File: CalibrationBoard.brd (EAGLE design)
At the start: 100 x 80 mm, 113 parts, among them J1 BANANA_CONN, J2 BANANA_CONN, J3 BANANA_CONN, J4 BANANA_CONN, J5 BANANA_CONN, J6 BANANA_CONN, J7 BANANA_CONN, J8 BANANA_CONN, J9 BANANA_CONN, Q1 IRF540, U1 MAX6126AASA25+, U2 MAX6126AASA25+, U3 MAX6126AASA50+

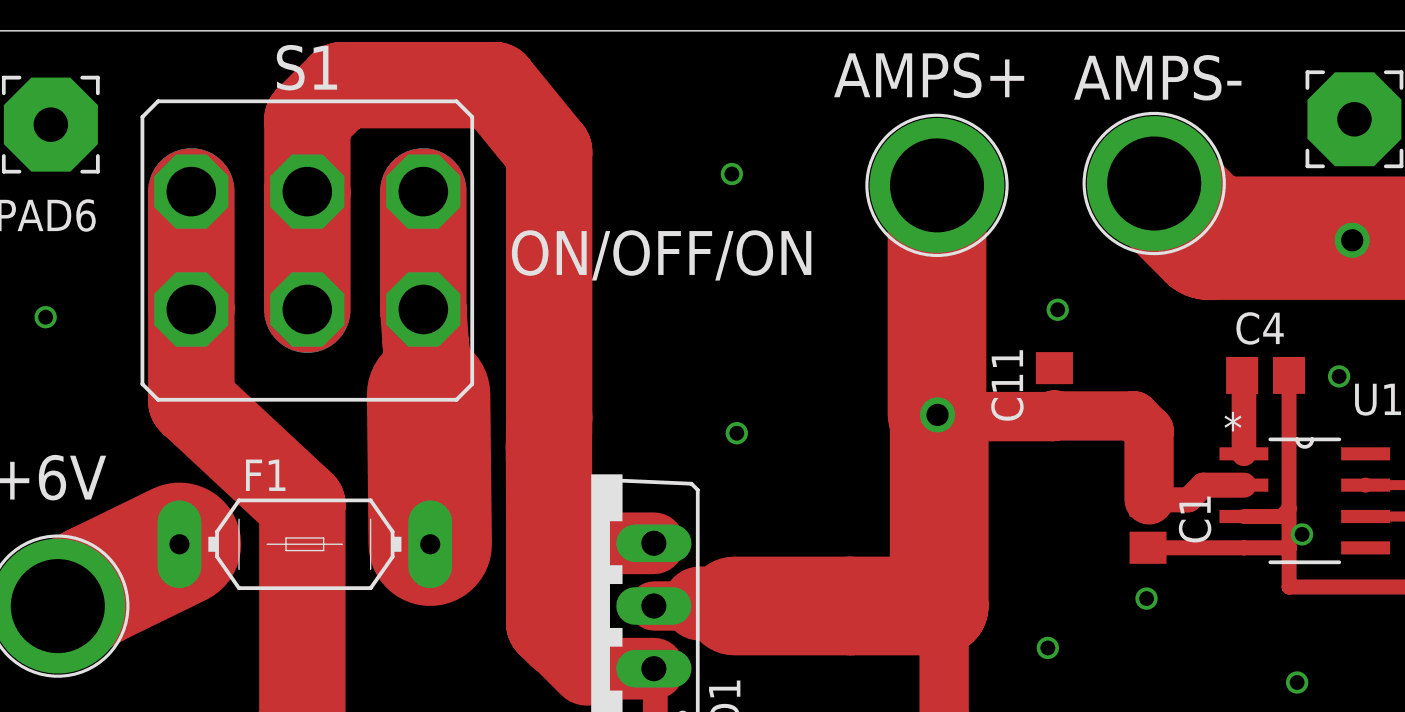
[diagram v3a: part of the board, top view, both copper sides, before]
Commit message: Various minor changes with minor CAD impacts
Connected some minor air nets (no CAD issues)
Changed NR caps from 1uF to 0.1uF as per DS.
Moved a decoupling cap to allow ground flood to IC.
Standardised the plane to track separation.
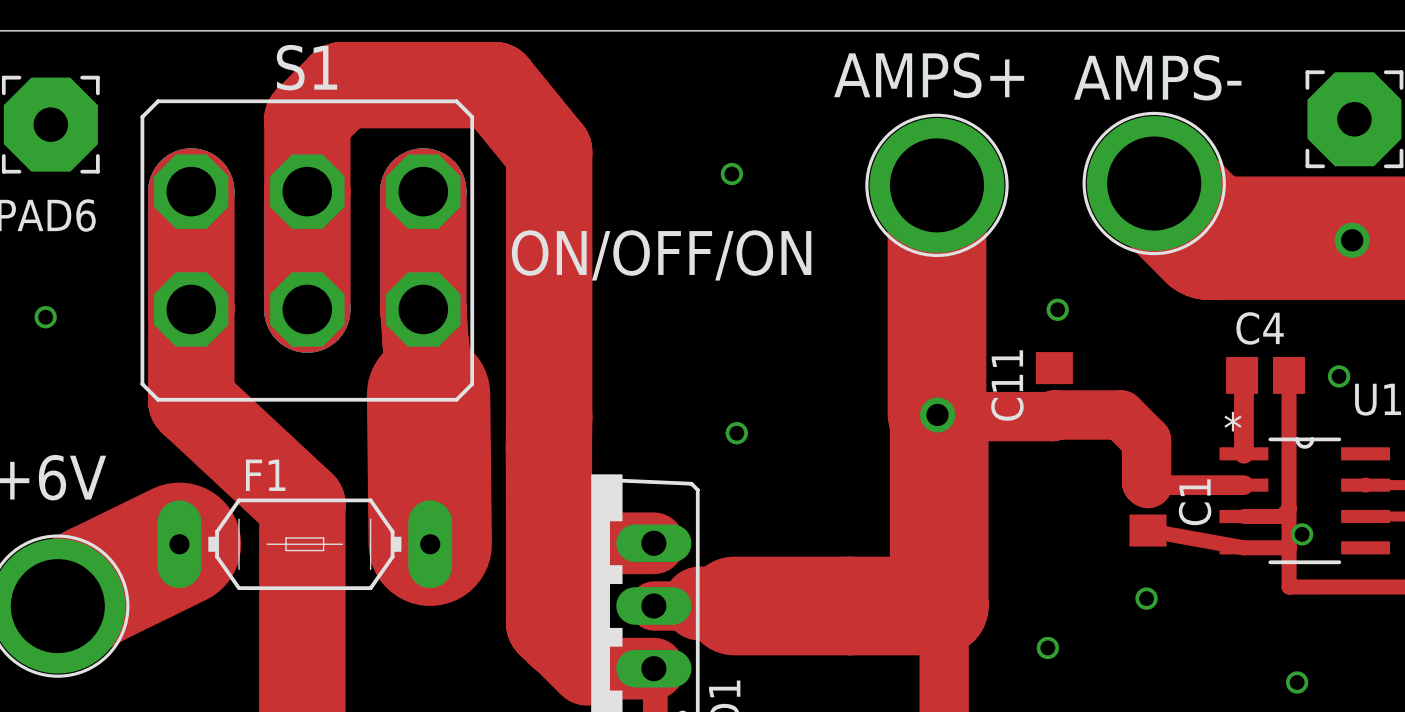
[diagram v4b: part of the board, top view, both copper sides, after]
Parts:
- C4, C5, C6: value 1uF -> 0.1uF
- R3: value 5R -> 25R
- moved C1 0.70 mm to (48.3, 60.7)
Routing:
- net V_IN_2: track 89.0 -> 87.9 mm
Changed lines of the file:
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@@
 <attribute name="MF" value="MAXIM INTEGRATED PRODUCTS" x="54.61" y="60.96" size="1.778" layer="27" display="off"/>
 </element>
-<element name="C1" library="rcl" package="C0805" value="2.2uF" x="48.26" y="60.0075" rot="R270">
-<attribute name="OC_FARNELL" value="unknown" x="48.26" y="60.0075" size="1.778" layer="27" rot="R270" display="off"/>
-<attribute name="MF" value="" x="48.26" y="60.0075" size="1.778" layer="27" rot="R270" display="off"/>
-<attribute name="MPN" value="" x="48.26" y="60.0075" size="1.778" layer="27" rot="R270" display="off"/>
-</element>
-<element name="C4" library="rcl" package="C0805" value="1uF" x="53.0225" y="66.04">
+<element name="C1" library="rcl" package="C0805" value="2.2uF" x="48.26" y="60.7075" rot="R270">
+<attribute name="OC_FARNELL" value="unknown" x="48.26" y="60.7075" size="1.778" layer="27" rot="R270" display="off"/>
+<attribute name="MF" value="" x="48.26" y="60.7075" size="1.778" layer="27" rot="R270" display="off"/>
+<attribute name="MPN" value="" x="48.26" y="60.7075" size="1.778" layer="27" rot="R270" display="off"/>
+</element>
+<element name="C4" library="rcl" package="C0805" value="0.1uF" x="53.0225" y="66.04">
 <attribute name="OC_FARNELL" value="unknown" x="53.0225" y="66.04" size="1.778" layer="27" display="off"/>
 <attribute name="MF" value="" x="53.0225" y="66.04" size="1.778" layer="27" display="off"/>
@@
 <attribute name="MPN" value="" x="60.325" y="58.42" size="1.778" layer="27" rot="R270" display="off"/>
 </element>
-<element name="R3" library="rcl" package="R0805" value="5R" x="63.8175" y="54.9275">
+<element name="R3" library="rcl" package="R0805" value="25R" x="63.8175" y="54.9275">
 <attribute name="OC_FARNELL" value="unknown" x="63.8175" y="54.9275" size="1.778" layer="27" display="off"/>
 <attribute name="MF" value="" x="63.8175" y="54.9275" size="1.778" layer="27" display="off"/>
@@
 <attribute name="MPN" value="" x="48.26" y="29.21" size="1.778" layer="27" rot="R270" display="off"/>
 </element>
-<element name="C5" library="rcl" package="C0805" value="1uF" x="53.0825" y="33.71">
+<element name="C5" library="rcl" package="C0805" value="0.1uF" x="53.0825" y="33.71">
 <attribute name="OC_FARNELL" value="unknown" x="53.0825" y="33.71" size="1.778" layer="27" display="off"/>
 <attribute name="MF" value="" x="53.0825" y="33.71" size="1.778" layer="27" display="off"/>
@@
 <attribute name="MPN" value="" x="48.26" y="44.1325" size="1.778" layer="27" rot="R270" display="off"/>
 </element>
-<element name="C6" library="rcl" package="C0805" value="1uF" x="53.1" y="48.87">
+<element name="C6" library="rcl" package="C0805" value="0.1uF" x="53.1" y="48.87">
 <attribute name="OC_FARNELL" value="unknown" x="53.1" y="48.87" size="1.778" layer="27" display="off"/>
 <attribute name="MF" value="" x="53.1" y="48.87" size="1.778" layer="27" display="off"/>
@@
 <wire x1="53.975" y1="59.055" x2="53.975" y2="57.4675" width="0.6096" layer="1"/>
 <wire x1="53.975" y1="57.4675" x2="60.325" y2="57.47" width="0.6096" layer="1"/>
-<wire x1="52.1462" y1="59.055" x2="48.26" y2="59.0575" width="0.6096" layer="1"/>
+<wire x1="52.1462" y1="59.055" x2="48.26" y2="59.7575" width="0.6096" layer="1"/>
 <wire x1="62.8675" y1="54.9275" x2="60.6425" y2="54.9275" width="1.016" layer="1"/>
 <wire x1="60.6425" y1="54.9275" x2="60.325" y2="55.245" width="1.016" layer="1"/>
@@
 <vertex x="102.87" y="-2.54"/>
 </polygon>
-<polygon width="0.4064" layer="16" isolate="0.6096" rank="3">
+<polygon width="0.4064" layer="16" isolate="0.4064" rank="3">
 <vertex x="-1.27" y="81.28"/>
 <vertex x="101.6" y="81.28"/>
@@
 <wire x1="59.3725" y1="60.325" x2="57.0738" y2="60.325" width="0.4064" layer="1"/>
 <contactref element="Q1" pad="S"/>
-<polygon width="0.254" layer="1" isolate="0.254">
+<polygon width="0.254" layer="1" isolate="0.4064">
 <vertex x="84.09" y="48.27"/>
 <vertex x="62.23" y="48.27"/>
@@
 <contactref element="U1" pad="1"/>
 <contactref element="C4" pad="1"/>
-<wire x1="52.1462" y1="62.865" x2="52.1462" y2="65.9663" width="1" layer="1"/>
+<wire x1="52.1462" y1="62.865" x2="52.1462" y2="65.9663" width="0.8" layer="1"/>
 <wire x1="52.1462" y1="65.9663" x2="52.0725" y2="66.04" width="1" layer="1"/>
 </signal>
@@
 <contactref element="J6" pad="P$1"/>
 <contactref element="TP4" pad="P$1"/>
-<polygon width="0.254" layer="1" isolate="0.6096" thermals="no" rank="2">
+<polygon width="0.254" layer="1" isolate="0.4064" thermals="no" rank="2">
 <vertex x="62.365" y="72.155"/>
 <vertex x="83.945" y="72.255"/>
@@
 <wire x1="52.1437" y1="45.0825" x2="52.1462" y2="45.085" width="0.8128" layer="1"/>
 <contactref element="D1" pad="C"/>
-<wire x1="52.1462" y1="61.595" x2="50.495" y2="61.595" width="1.016" layer="1"/>
-<wire x1="50.495" y1="61.595" x2="49.9" y2="61" width="1.016" layer="1"/>
-<wire x1="49.9" y1="61" x2="48.3025" y2="61" width="1.016" layer="1"/>
-<wire x1="48.3025" y1="61" x2="48.26" y2="60.9575" width="1.016" layer="1"/>
 <wire x1="30.1" y1="56.8" x2="30.6" y2="56.8" width="3" layer="1"/>
 <wire x1="30.6" y1="56.8" x2="31.4" y2="56.8" width="3" layer="1"/>
@@
 <wire x1="36.2" y1="56.7" x2="39.8" y2="56.7" width="4" layer="1"/>
 <wire x1="39.71" y1="73.74" x2="39.71" y2="64.4625" width="4" layer="1"/>
-<wire x1="48.3025" y1="61" x2="48.3025" y2="63.7975" width="2" layer="1"/>
-<wire x1="48.3025" y1="63.7975" x2="47.7" y2="64.4" width="2" layer="1"/>
-<wire x1="47.7" y1="64.4" x2="44.505" y2="64.4" width="2" layer="1"/>
-<wire x1="44.505" y1="64.4" x2="44.4675" y2="64.4375" width="2" layer="1"/>
 <wire x1="44.4025" y1="64.3725" x2="44.4675" y2="64.4375" width="2" layer="1"/>
 <wire x1="48.26" y1="30.16" x2="46.24" y2="30.16" width="2" layer="1"/>
@@
 <wire x1="28.24" y1="56.7" x2="30.5" y2="56.7" width="2" layer="1"/>
 <wire x1="30.5" y1="56.7" x2="30.6" y2="56.8" width="2" layer="1"/>
-<wire x1="39.7325" y1="64.44" x2="39.71" y2="64.4625" width="0" layer="19" extent="1-1"/>
+<wire x1="39.7325" y1="64.44" x2="39.71" y2="64.4625" width="1" layer="1"/>
+<wire x1="44.4675" y1="64.4375" x2="47.1625" y2="64.4375" width="2" layer="1"/>
+<wire x1="47.1625" y1="64.4375" x2="48.2" y2="63.4" width="2" layer="1"/>
+<wire x1="48.2" y1="63.4" x2="48.2" y2="61.7175" width="2" layer="1"/>
+<wire x1="48.2" y1="61.7175" x2="48.26" y2="61.6575" width="2" layer="1"/>
+<wire x1="52.1462" y1="61.595" x2="48.3225" y2="61.595" width="0.8" layer="1"/>
+<wire x1="48.3225" y1="61.595" x2="48.26" y2="61.6575" width="0.8" layer="1"/>
 </signal>
 <signal name="N$22">
@@
 <wire x1="19.1132" y1="66.4868" x2="19" y2="67.3" width="3.5" layer="1"/>
 <wire x1="19" y1="67.3" x2="18.9" y2="68.7124" width="3.5" layer="1"/>
-<wire x1="18.9" y1="73.5" x2="18.9" y2="68.7" width="3.5" layer="16"/>
-<wire x1="18.9" y1="73.4876" x2="18.9" y2="73.5" width="0" layer="19" extent="16-16"/>
+<wire x1="18.9" y1="73.5" x2="18.9" y2="73.4876" width="3.5" layer="16"/>
+<wire x1="18.9" y1="73.4876" x2="18.9" y2="68.7" width="3.5" layer="16"/>
 </signal>
 <signal name="N$9">
@@
 <wire x1="9.5" y1="68.7124" x2="9.5" y2="73.4876" width="3.5" layer="1"/>
 <wire x1="9.5" y1="68.7124" x2="9.5" y2="65" width="3.5" layer="1"/>
-<wire x1="9.5" y1="73.5" x2="9.5" y2="68.7" width="3.5" layer="16"/>
-<wire x1="9.5" y1="73.4876" x2="9.5" y2="73.5" width="0" layer="19" extent="16-16"/>
+<wire x1="9.5" y1="73.5" x2="9.5" y2="73.4876" width="3.5" layer="16"/>
+<wire x1="9.5" y1="73.4876" x2="9.5" y2="68.7" width="3.5" layer="16"/>
 </signal>
 <signal name="N$30">
@@
 <wire x1="21.8" y1="77.8" x2="24" y2="75.1" width="3.5" layer="1"/>
 <wire x1="24" y1="75.1" x2="24" y2="64.3264" width="3.5" layer="1"/>
-<wire x1="14.2" y1="73.4" x2="14.2" y2="68.7" width="3.5" layer="16"/>
+<wire x1="14.2" y1="73.4" x2="14.2" y2="68.7124" width="3.5" layer="16"/>
+<wire x1="14.2" y1="68.7124" x2="14.2" y2="68.7" width="3.5" layer="16"/>
 <wire x1="28.3" y1="51.6" x2="28.3" y2="51.5" width="1.016" layer="1"/>
 <wire x1="28.3" y1="51.5" x2="29.7" y2="50.1" width="1.016" layer="1"/>
@@
 <wire x1="35.8" y1="50.1" x2="36.7" y2="49.2" width="1.016" layer="1"/>
 <wire x1="36.7" y1="49.2" x2="36.7" y2="47.35" width="1.016" layer="1"/>
-<wire x1="14.2" y1="68.7124" x2="14.2" y2="68.7" width="0" layer="19" extent="16-16"/>
 </signal>
 <signal name="N$32">

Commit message: latest commits
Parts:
- BAT1: value +9V_BATTERY -> +9V_BATTERY_HOLDER
- C12: value 10pF -> 47pF
- C13: value 1nF -> 1.2nF
- J1, J3, J4, J5, J7: value BANANA_CONN -> BANANA_CONN_RED
- J2, J6, J8, J9: value BANANA_CONN -> BANANA_CONN_BLACK
- L5: value 10mH -> 4.7mH
- LED1: value GREEN_LED -> RED_LED
- Q1: value IRF540 -> IRF3708PBF
- moved C14 2.30 mm to (45.3, 14.5)
- moved TP10 2.30 mm to (41.8, 14.5)
- moved TP12 2.30 mm to (41.9, 10.0)
- moved TP15 2.30 mm to (48.3, 18.9)
- moved TP17 2.30 mm to (48.3, 14.5)
- moved C12 2.30 mm to (45.2, 18.9)
- moved C16 2.30 mm to (45.5, 10.0)
- moved TP19 2.30 mm to (48.5, 10.0)
- moved TP8 2.30 mm to (41.7, 18.9)
- moved TP46 0.30 mm to (27.0, 4.90)

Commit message: latest updates
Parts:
- removed J9: BANANA_CONN_BLACK, SparkFun-Connectors:BANANA_CONN
- removed PAD1, PAD2, PAD3, PAD4, PAD5, PAD6: MOUNT_HOLE, wirepad:3,81/1,4
- added C19: 100uF, rcl:E5-10,5
- added H1, H2, H3, H4: MOUNT-PAD-ROUND3.3, holes:3,3-PAD
- F1: device fuse:LITTLEFUSE -> RGEF1200:RGEF1200
- moved J8 13.9 mm to (94.3, 51.7)
- moved TP43 8.31 mm to (49.2, 4.60)
- moved TP48 8.31 mm to (58.6, 4.60)
- moved L4 8.31 mm to (53.8, 4.60)
- moved R1 7.93 mm to (29.0, 44.5), turned to 180 degrees
- moved J7 7.43 mm to (94.5, 63.8)
- moved L3 7.11 mm to (41.1, 4.50)
- moved TP42 7.11 mm to (36.6, 4.50)
- moved TP47 7.11 mm to (45.5, 4.50)
- moved F1 6.85 mm to (19.8, 55.4)
- moved L2 5.91 mm to (29.2, 4.50)
- moved TP41 5.91 mm to (25.4, 4.50)
- moved TP46 5.91 mm to (32.9, 4.50)
- moved S1 5.82 mm to (19.9, 69.9)
- moved F2 5.56 mm to (14.4, 40.2), turned to 0 degrees
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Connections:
- net GND: now also C19.-, H1.B3,3, H2.B3,3, H3.B3,3, H4.B3,3; no longer J9.P$1, PAD1.1, PAD2.1, PAD3.1, PAD4.1, PAD5.1, PAD6.1
- net V_IN_2: now also C19.+
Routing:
- net V_IN_B: track 34.2 -> 41.8 mm
- net +6V_IN: track 5.53 -> 11.0 mm
- net OUTS: track 46.1 -> 50.8 mm
- net I_METER-: track 29.8 -> 34.4 mm
- net +2.5V_REF: track 42.8 -> 45.6 mm
- net V_IN_A: track 19.1 -> 21.8 mm
- net +5.0V_REF: track 43.0 -> 45.0 mm
- net N$9: track 8.30 -> 10.2 mm
- net V_IN_1: track 72.6 -> 70.8 mm
- net V_IN_2: track 87.9 -> 89.6 mm
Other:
- board text added: "CAD B"
- board text added: "GND/LOAD-"
- board text removed: "CAD A"
- board text removed: "LOAD-"
